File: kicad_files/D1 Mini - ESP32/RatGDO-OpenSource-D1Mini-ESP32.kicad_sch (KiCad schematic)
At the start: 9 parts, among them J1 Screw_Terminal_01x03, J2 Screw_Terminal_01x03, J3 Screw_Terminal_01x03, Q1 2N7002, Q2 AO3400A, U1 mini_esp32

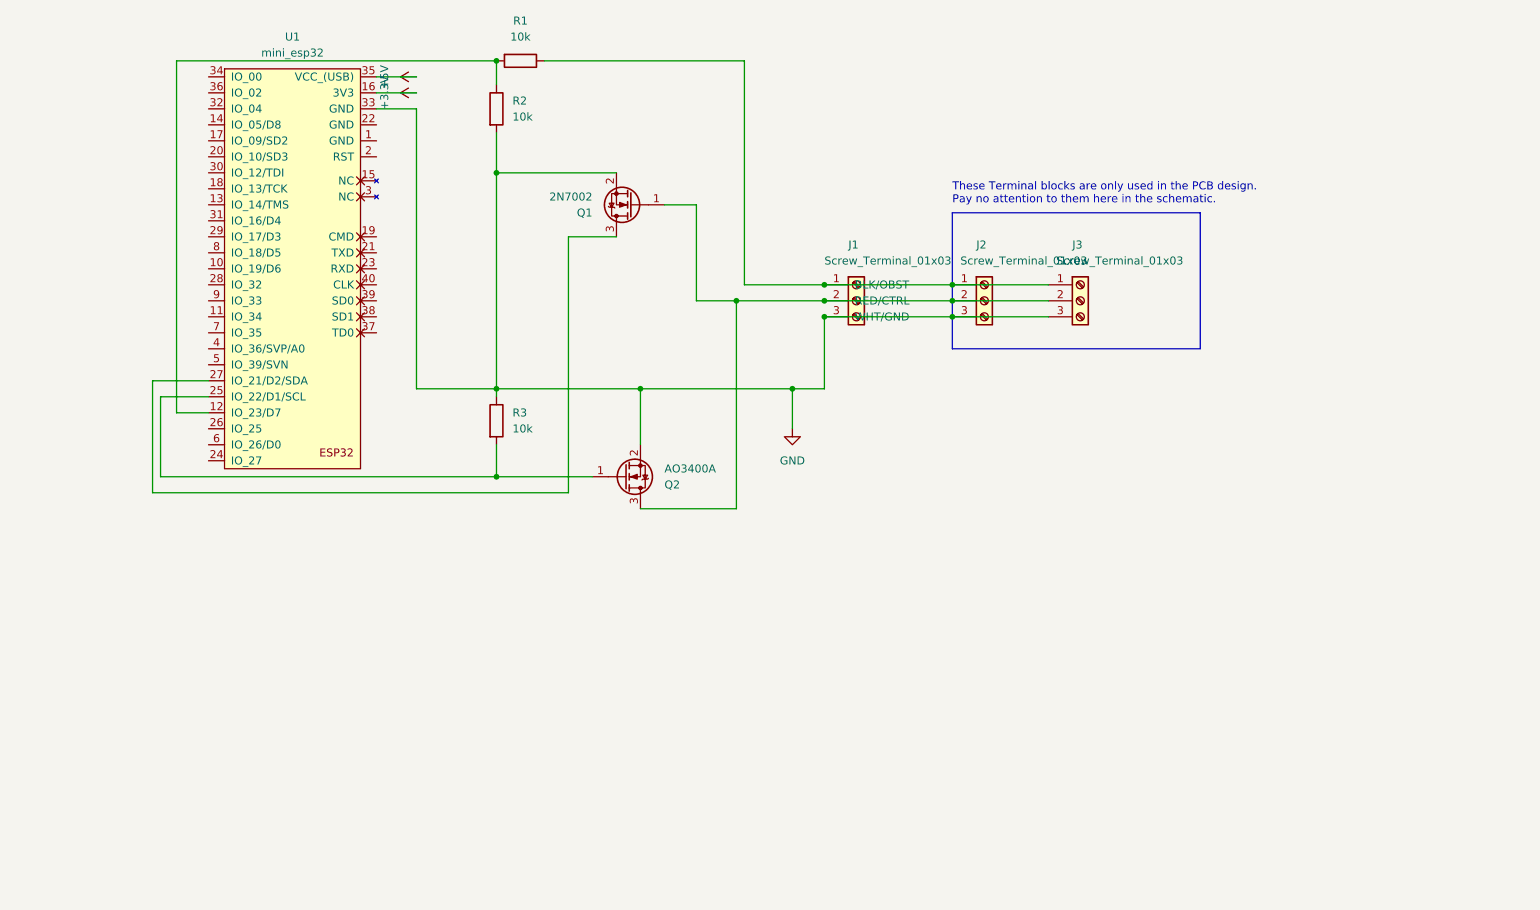
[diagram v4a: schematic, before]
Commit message: Update ESP32 Mini schematics and PCB
Added 1K R4 on gate of Q2.
Added 10K R5/R6 on gate of Q1.
Re-laid out PCB, all single sided and smaller.
Changed pads to hand solder.
Modified from ESP8266 layout.
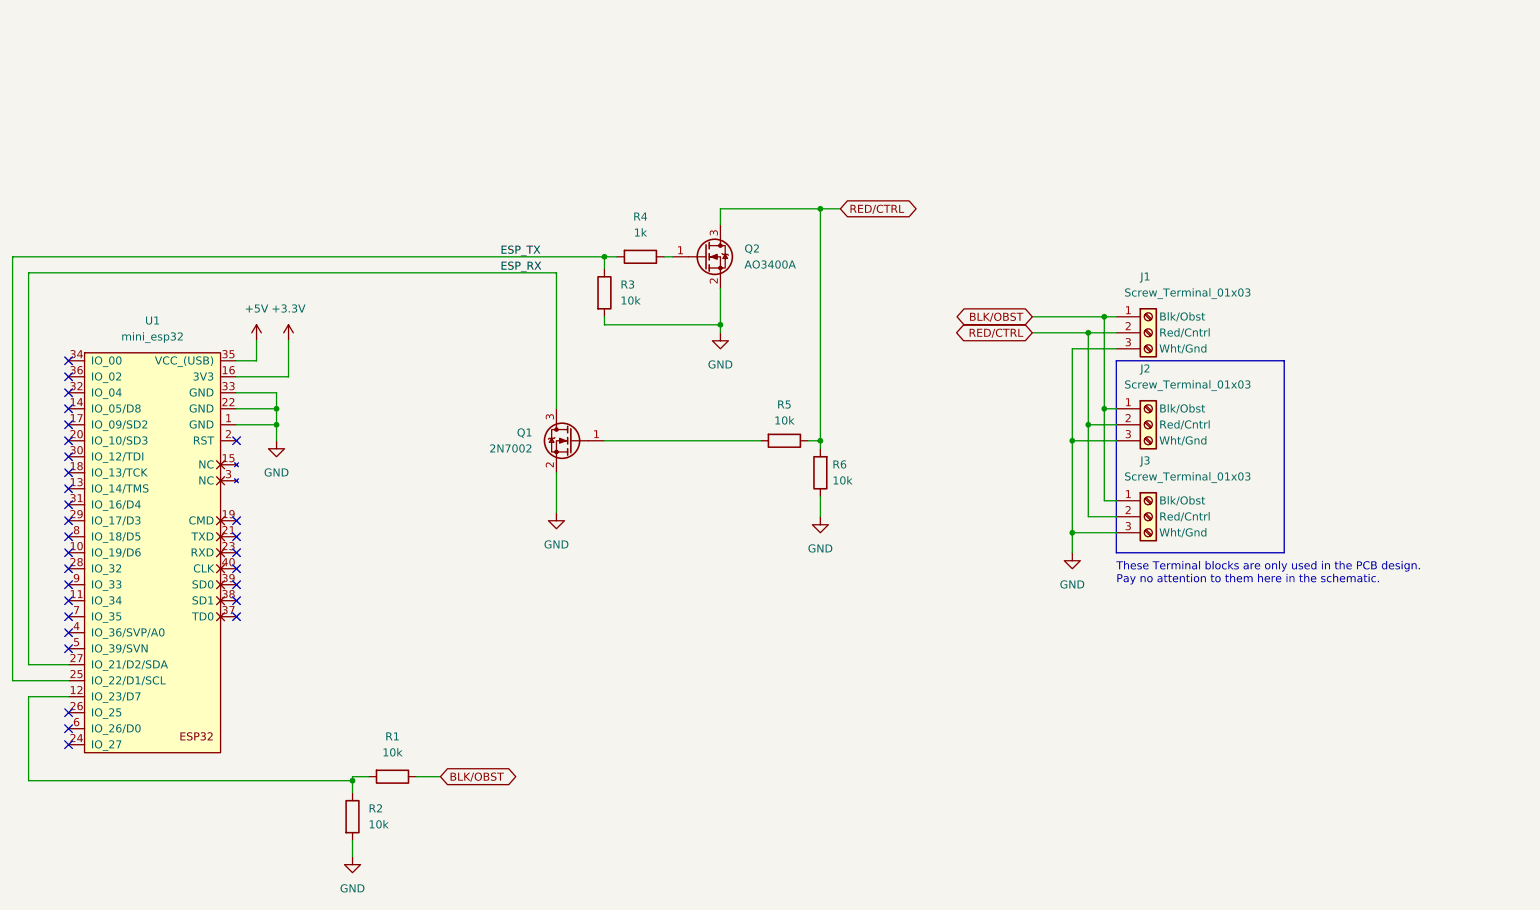
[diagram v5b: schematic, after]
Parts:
- added R4: 1k, Resistor_SMD:R_0805_2012Metric_Pad1.20x1.40mm_HandSolder, symbol Device:R
- added R5, R6: 10k, Resistor_SMD:R_0805_2012Metric_Pad1.20x1.40mm_HandSolder, symbol Device:R
- J3: footprint Connector_PinSocket_2.54mm:PinSocket_1x03_P2.54mm_Vertical -> Connector_PinHeader_2.54mm:PinHeader_1x03_P2.54mm_Vertical
- Q1, Q2: footprint Package_TO_SOT_SMD:SOT-23 -> Package_TO_SOT_SMD:SOT-23_Handsoldering
- R1, R2, R3: footprint Resistor_SMD:R_0805_2012Metric -> Resistor_SMD:R_0805_2012Metric_Pad1.20x1.40mm_HandSolder
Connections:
- net GND: now also R3.2, U1.1 (GND), U1.22 (GND), R6.1; no longer R3.1
- net ESP_RX: now reaches Q1.3 (D), U1.27 (IO_21/D2/SDA)
- net BLK/OBST: now reaches J1.1 (Blk/Obst), J2.1 (Blk/Obst), J3.1 (Blk/Obst), R1.1
- net RED/CTRL: now reaches J1.2 (Red/Cntrl), J2.2 (Red/Cntrl), J3.2 (Red/Cntrl), Q2.3 (D)
- net RED/CTRL: now also R5.1, R6.2; no longer Q1.1 (G)
- new net: Q1.1 (G), R5.2
- new net: Q2.1 (G), R4.1
- new net ESP_TX: R3.1, R4.2, U1.25 (IO_22/D1/SCL)
- no-connect marks 0 -> 30
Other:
- title: (none) -> RatGDO OpenSource D1Mini-ESP32
- moved on the sheet: J1, Q1, Q2, R1, R2, R3

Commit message: Update schematics for mini wide board v2.5
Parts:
- J1: LCSC# (none) -> C8483
- Q1: LCSC# (none) -> C8545
- Q2: LCSC# (none) -> C20917
- R1, R2, R3, R5, R6: LCSC# (none) -> C17414
- R4: LCSC# (none) -> C17513
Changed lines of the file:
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@@
+      (effects (font (size 1.27 1.27)) hide)
+    )
+    (property "LCSC#" "C17414" (at 156.845 117.475 0)
       (effects (font (size 1.27 1.27)) hide)
     )
@@
     )
     (property "Datasheet" "~" (at 122.555 88.9 0)
+      (effects (font (size 1.27 1.27)) hide)
+    )
+    (property "LCSC#" "C17414" (at 105.41 109.22 0)
       (effects (font (size 1.27 1.27)) hide)
     )
@@
       (effects (font (size 1.27 1.27)) hide)
     )
+    (property "LCSC#" "C8483" (at 162.56 90.17 0)
+      (effects (font (size 1.27 1.27)) hide)
+    )
     (pin "1")
     (pin "2")
@@
       (effects (font (size 1.27 1.27)) hide)
     )
+    (property "LCSC#" "C17414" (at 105.41 59.69 0)
+      (effects (font (size 1.27 1.27)) hide)
+    )
     (pin "1")
     (pin "2")
@@
       (effects (font (size 1.27 1.27)) hide)
     )
+    (property "LCSC#" "C17414" (at 151.13 112.395 90)
+      (effects (font (size 1.27 1.27)) hide)
+    )
     (pin "1")
     (pin "2")
@@
     )
     (property "Datasheet" "~" (at 128.27 83.185 0)
+      (effects (font (size 1.27 1.27)) hide)
+    )
+    (property "LCSC#" "C17513" (at 128.27 83.185 90)
       (effects (font (size 1.27 1.27)) hide)
     )
@@
       (effects (font (size 1.27 1.27)) (justify left) hide)
     )
+    (property "LCSC#" "C20917" (at 125.73 118.11 0)
+      (effects (font (size 1.27 1.27)) hide)
+    )
     (pin "1")
     (pin "2")
@@
     )
     (property "Datasheet" "~" (at 88.9 165.735 0)
+      (effects (font (size 1.27 1.27)) hide)
+    )
+    (property "LCSC#" "C17414" (at 109.22 52.07 90)
       (effects (font (size 1.27 1.27)) hide)
     )
@@
       (effects (font (size 1.27 1.27)) (justify left) hide)
     )
-    (pin "1")
+    (property "LCSC#" "C8545" (at 127 74.93 0)
+      (effects (font (size 1.27 1.27)) hide)
+    )
+    (pin "1")
